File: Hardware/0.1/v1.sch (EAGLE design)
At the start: 23 parts, among them K1 ZF112, K2 ZF112, K3 ZF112, K4 ZF112

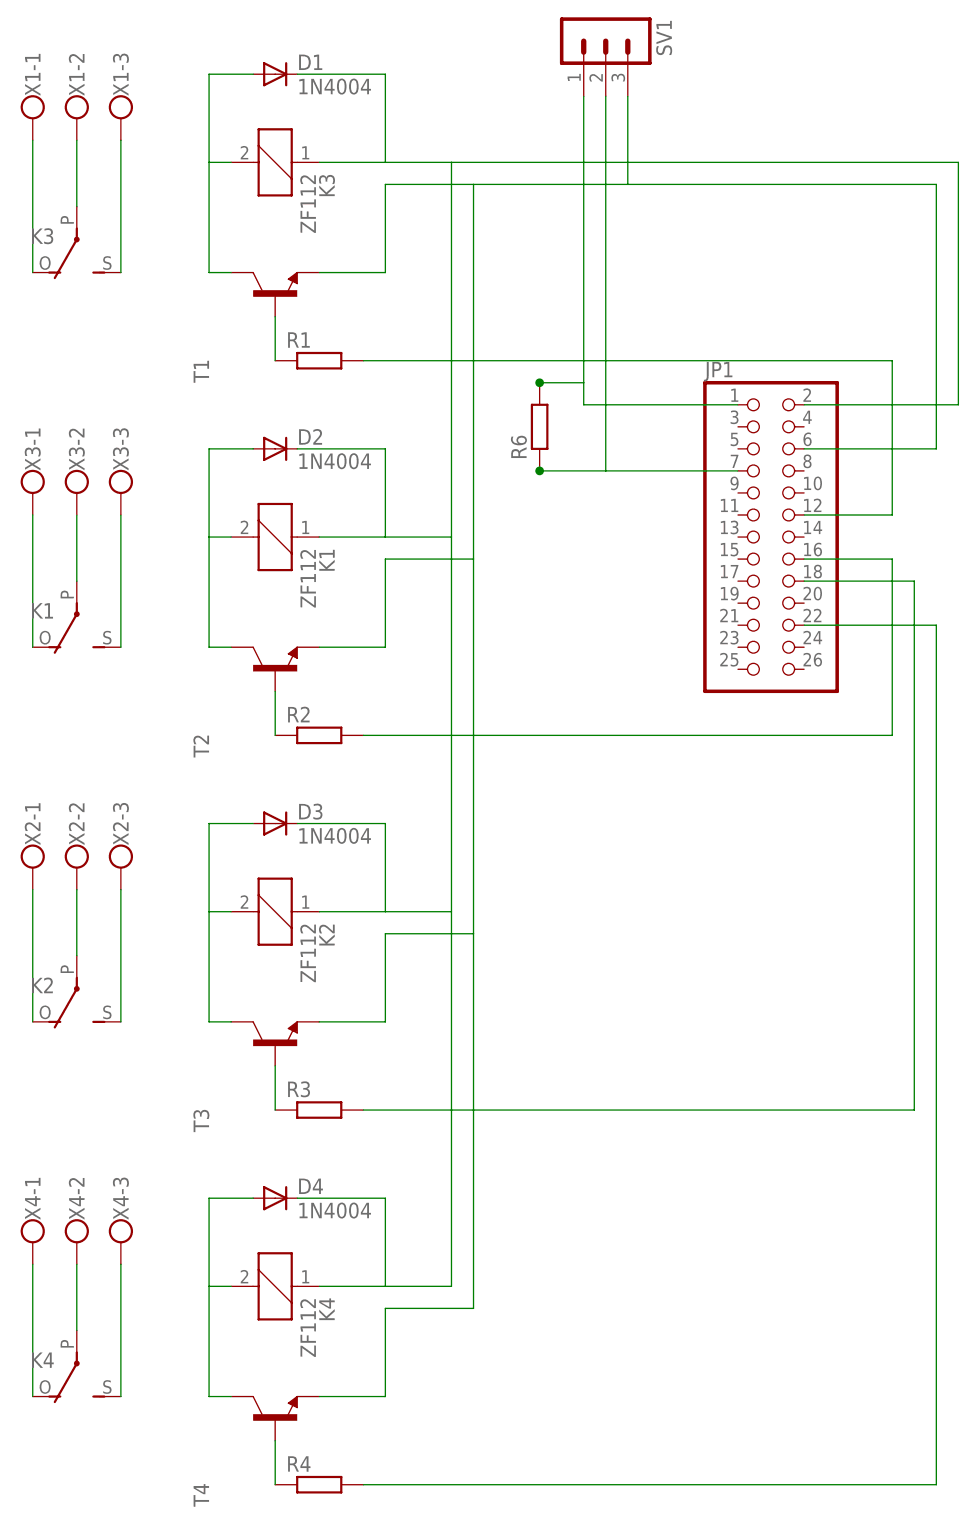
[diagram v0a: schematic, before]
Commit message: wartości na schemacie
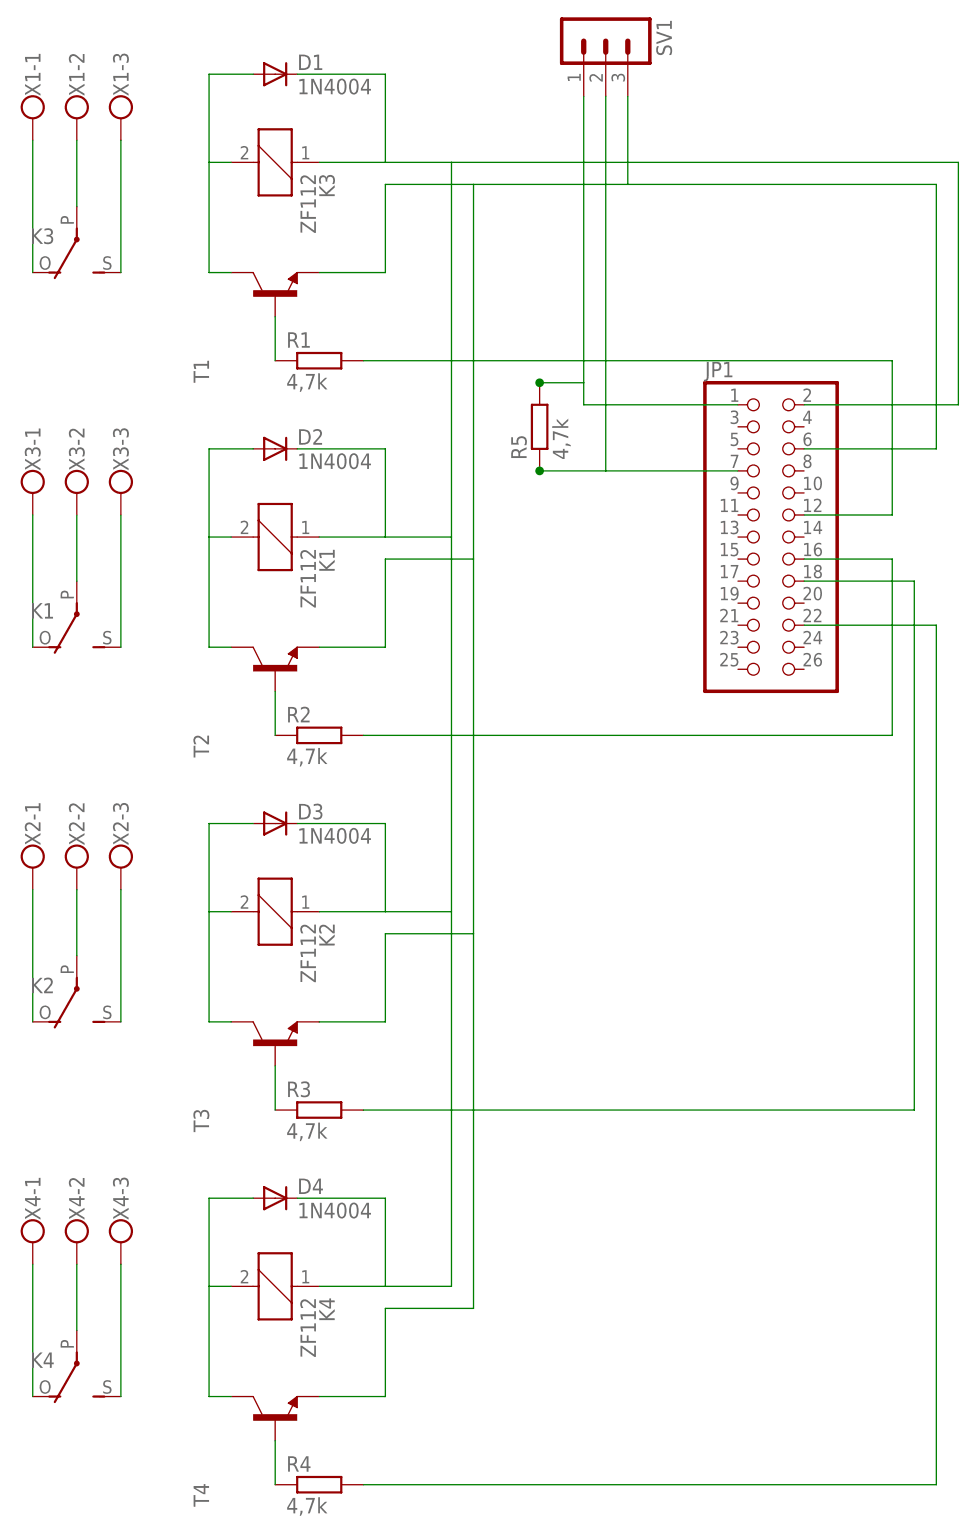
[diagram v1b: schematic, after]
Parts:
- R1, R2, R3, R4, R5: value (none) -> 4,7k
- renumbered R6 to R5
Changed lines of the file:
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@@
 <?xml version="1.0" encoding="utf-8"?>
 <!DOCTYPE eagle SYSTEM "eagle.dtd">
-<eagle version="6.2">
+<eagle version="6.1">
 <drawing>
 <settings>
@@
 <part name="X3" library="con-wago-500" deviceset="W237-103" device=""/>
 <part name="JP1" library="pinhead" deviceset="PINHD-2X13" device=""/>
-<part name="R1" library="rcl" deviceset="R-EU_" device="0204/7"/>
-<part name="R2" library="rcl" deviceset="R-EU_" device="0204/7"/>
+<part name="R1" library="rcl" deviceset="R-EU_" device="0204/7" value="4,7k"/>
+<part name="R2" library="rcl" deviceset="R-EU_" device="0204/7" value="4,7k"/>
 <part name="K3" library="relay" deviceset="ZF112" device=""/>
 <part name="K1" library="relay" deviceset="ZF112" device=""/>
@@
 <part name="T3" library="transistor" deviceset="*-NPN-" device="TO92-ECB" technology="BC639"/>
 <part name="X2" library="con-wago-500" deviceset="W237-103" device=""/>
-<part name="R3" library="rcl" deviceset="R-EU_" device="0204/7"/>
+<part name="R3" library="rcl" deviceset="R-EU_" device="0204/7" value="4,7k"/>
 <part name="K2" library="relay" deviceset="ZF112" device=""/>
 <part name="D4" library="diode" deviceset="1N4004" device=""/>
 <part name="T4" library="transistor" deviceset="*-NPN-" device="TO92-ECB" technology="BC639"/>
 <part name="X4" library="con-wago-500" deviceset="W237-103" device=""/>
-<part name="R4" library="rcl" deviceset="R-EU_" device="0204/7"/>
+<part name="R4" library="rcl" deviceset="R-EU_" device="0204/7" value="4,7k"/>
 <part name="K4" library="relay" deviceset="ZF112" device=""/>
 <part name="SV1" library="con-lstb" deviceset="MA03-1" device=""/>
-<part name="R6" library="rcl" deviceset="R-EU_" device="0207/7"/>
+<part name="R5" library="rcl" deviceset="R-EU_" device="0207/7" value="4,7k"/>
 </parts>
 <sheets>
@@
 <instance part="K4" gate="2" x="38.1" y="-66.04" rot="R180"/>
 <instance part="SV1" gate="G$1" x="99.06" y="86.36" rot="R270"/>
-<instance part="R6" gate="G$1" x="91.44" y="40.64" rot="R90"/>
+<instance part="R5" gate="G$1" x="91.44" y="40.64" rot="R90"/>
 </instances>
 <busses>
@@
 <wire x1="96.52" y1="43.18" x2="96.52" y2="45.72" width="0.1524" layer="91"/>
 <wire x1="96.52" y1="45.72" x2="96.52" y2="78.74" width="0.1524" layer="91"/>
-<pinref part="R6" gate="G$1" pin="2"/>
+<pinref part="R5" gate="G$1" pin="2"/>
 <wire x1="91.44" y1="45.72" x2="96.52" y2="45.72" width="0.1524" layer="91"/>
 <junction x="91.44" y="45.72"/>
@@
 <wire x1="114.3" y1="35.56" x2="99.06" y2="35.56" width="0.1524" layer="91"/>
 <wire x1="99.06" y1="35.56" x2="99.06" y2="78.74" width="0.1524" layer="91"/>
-<pinref part="R6" gate="G$1" pin="1"/>
+<pinref part="R5" gate="G$1" pin="1"/>
 <wire x1="91.44" y1="35.56" x2="99.06" y2="35.56" width="0.1524" layer="91"/>
 <junction x="91.44" y="35.56"/>

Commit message: dopisane kolejne wartości
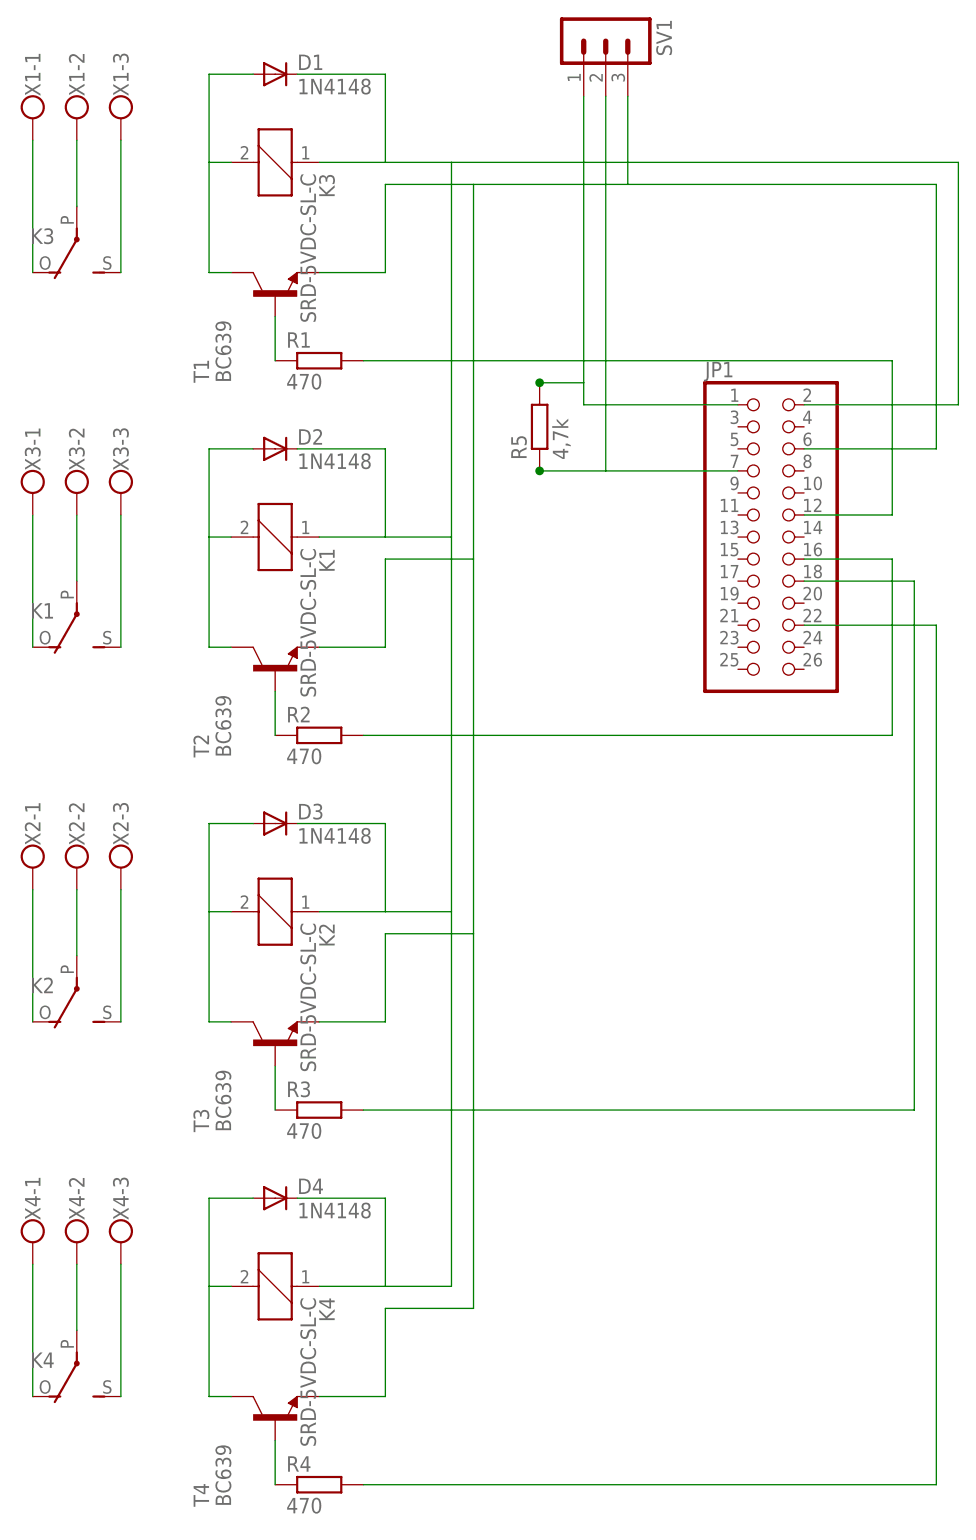
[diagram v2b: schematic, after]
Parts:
- D1, D2, D3, D4: value 1N4004 -> 1N4148
- K1, K2, K3, K4: value ZF112 -> SRD-5VDC-SL-C
- R1, R2, R3, R4: value 4,7k -> 470
- T1, T2, T3, T4: value (none) -> BC639
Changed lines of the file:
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@@
 </classes>
 <parts>
-<part name="D1" library="diode" deviceset="1N4004" device=""/>
-<part name="T1" library="transistor" deviceset="*-NPN-" device="TO92-ECB" technology="BC639"/>
+<part name="D1" library="diode" deviceset="1N4004" device="" value="1N4148"/>
+<part name="T1" library="transistor" deviceset="*-NPN-" device="TO92-ECB" technology="BC639" value="BC639"/>
 <part name="X1" library="con-wago-500" deviceset="W237-103" device=""/>
-<part name="D2" library="diode" deviceset="1N4004" device=""/>
-<part name="T2" library="transistor" deviceset="*-NPN-" device="TO92-ECB" technology="BC639"/>
+<part name="D2" library="diode" deviceset="1N4004" device="" value="1N4148"/>
+<part name="T2" library="transistor" deviceset="*-NPN-" device="TO92-ECB" technology="BC639" value="BC639"/>
 <part name="X3" library="con-wago-500" deviceset="W237-103" device=""/>
 <part name="JP1" library="pinhead" deviceset="PINHD-2X13" device=""/>
-<part name="R1" library="rcl" deviceset="R-EU_" device="0204/7" value="4,7k"/>
-<part name="R2" library="rcl" deviceset="R-EU_" device="0204/7" value="4,7k"/>
-<part name="K3" library="relay" deviceset="ZF112" device=""/>
-<part name="K1" library="relay" deviceset="ZF112" device=""/>
-<part name="D3" library="diode" deviceset="1N4004" device=""/>
-<part name="T3" library="transistor" deviceset="*-NPN-" device="TO92-ECB" technology="BC639"/>
+<part name="R1" library="rcl" deviceset="R-EU_" device="0204/7" value="470"/>
+<part name="R2" library="rcl" deviceset="R-EU_" device="0204/7" value="470"/>
+<part name="K3" library="relay" deviceset="ZF112" device="" value="SRD-5VDC-SL-C"/>
+<part name="K1" library="relay" deviceset="ZF112" device="" value="SRD-5VDC-SL-C"/>
+<part name="D3" library="diode" deviceset="1N4004" device="" value="1N4148"/>
+<part name="T3" library="transistor" deviceset="*-NPN-" device="TO92-ECB" technology="BC639" value="BC639"/>
 <part name="X2" library="con-wago-500" deviceset="W237-103" device=""/>
-<part name="R3" library="rcl" deviceset="R-EU_" device="0204/7" value="4,7k"/>
-<part name="K2" library="relay" deviceset="ZF112" device=""/>
-<part name="D4" library="diode" deviceset="1N4004" device=""/>
-<part name="T4" library="transistor" deviceset="*-NPN-" device="TO92-ECB" technology="BC639"/>
+<part name="R3" library="rcl" deviceset="R-EU_" device="0204/7" value="470"/>
+<part name="K2" library="relay" deviceset="ZF112" device="" value="SRD-5VDC-SL-C"/>
+<part name="D4" library="diode" deviceset="1N4004" device="" value="1N4148"/>
+<part name="T4" library="transistor" deviceset="*-NPN-" device="TO92-ECB" technology="BC639" value="BC639"/>
 <part name="X4" library="con-wago-500" deviceset="W237-103" device=""/>
-<part name="R4" library="rcl" deviceset="R-EU_" device="0204/7" value="4,7k"/>
-<part name="K4" library="relay" deviceset="ZF112" device=""/>
+<part name="R4" library="rcl" deviceset="R-EU_" device="0204/7" value="470"/>
+<part name="K4" library="relay" deviceset="ZF112" device="" value="SRD-5VDC-SL-C"/>
 <part name="SV1" library="con-lstb" deviceset="MA03-1" device=""/>
 <part name="R5" library="rcl" deviceset="R-EU_" device="0207/7" value="4,7k"/>
